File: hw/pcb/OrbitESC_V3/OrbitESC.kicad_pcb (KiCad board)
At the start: 8 copper layers, 39.9 x 25.1 mm, 159 parts, among them J1 USB_C_Receptacle_USB2.0, J11 VDC, J12 GND, J3 TermA, J4 TermB, J5 TermC, J6 CAN1, Q1 MCAC100N08YA-TP, Q2 MCAC100N08YA-TP, Q3 MCAC100N08YA-TP, Q4 MCAC100N08YA-TP, Q5 MCAC100N08YA-TP, Q6 MCAC100N08YA-TP, Q7 2N7002, SW1 Reset, U1 TLE9250X, U10 CP2104, U11 STM32L432KCU6, U12 74HC595BQ, U13 TLV9051IDBVR, U14 TLV9051IDBVR, U2 AT25SF128A-SHB-T, U4 TLV9051IDBVR, U5 DRV8300DRGER, U7 AP62200Z6-7, U8 AP2171W, U9 AP2120

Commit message: save pcb work
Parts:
- added J2: CANH, TestPoint:TestPoint_Pad_1.5x1.5mm, B.Cu at (161.3, 65.5)
- added J7: CANL, TestPoint:TestPoint_Pad_1.5x1.5mm, B.Cu at (161.3, 67.4)
- added J8: RX, TestPoint:TestPoint_Pad_1.5x1.5mm, B.Cu at (166.4, 69.3)
- added J9: TX, TestPoint:TestPoint_Pad_1.5x1.5mm, B.Cu at (164.5, 69.3)
- J6: value CAN1 -> GND; footprint Connector_JST:JST_PH_B3B-PH-K_1x03_P2.00mm_Vertical -> TestPoint:TestPoint_Pad_1.5x1.5mm; moved to B.Cu
- U1, U9: moved to B.Cu
- moved C28 66.9 mm to (172.8, 66.9), turned to -90 degrees
- moved R17 65.8 mm to (169.4, 65.5), turned to 90 degrees
- moved C27 65.6 mm to (171.8, 66.9), turned to 90 degrees
- moved C29 62.3 mm to (168.1, 68.6), turned to -90 degrees
- moved C36 62.0 mm to (167.1, 68.6), turned to 90 degrees
- moved U1 61.9 mm to (165.5, 66.2), turned to 180 degrees
- moved U9 60.2 mm to (169.6, 66.5), turned to 180 degrees
- moved R62 58.2 mm to (162.8, 69.1)
- moved FB1 54.4 mm to (169.4, 68.1), turned to 90 degrees
- moved C10 52.9 mm to (167.6, 66.0), turned to -90 degrees
- moved C26 49.9 mm to (164.3, 70.6)
- moved L3 49.3 mm to (171.7, 65.2)
- moved L2 46.7 mm to (163.3, 66.5)
- moved R37 9.66 mm to (172.7, 88.4), turned to 90 degrees
- moved J6 9.49 mm to (161.3, 69.3), turned to 180 degrees
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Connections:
- J6 pad 1: Net-(J6-Pin_1) -> GND
- R62 pad 1: Net-(J6-Pin_3) -> Net-(J7-Pin_1)
- R62 pad 2: Net-(J6-Pin_1) -> Net-(J2-Pin_1)
- U1 pad 6: Net-(J6-Pin_3) -> Net-(J7-Pin_1)
- U1 pad 7: Net-(J6-Pin_1) -> Net-(J2-Pin_1)
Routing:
- net GND: track 0.00 -> 18.7 mm, vias 12 -> 23
- net CAN1_TXD: track 0.00 -> 11.9 mm
- net VDC: track 0.00 -> 11.6 mm, vias 0 -> 4
- net VBUS: track 0.00 -> 11.4 mm
- net Net-(J1-CC1): track 0.00 -> 8.33 mm, vias 0 -> 1
- net Net-(Q7-D): track 0.00 -> 8.18 mm, vias 0 -> 2
- net Net-(J1-CC2): track 0.00 -> 8.13 mm, vias 0 -> 1
- net +3.3V: track 0.00 -> 6.95 mm, vias 0 -> 2
- net Net-(J2-Pin_1): track 0.00 -> 6.88 mm, vias 0 -> 1
- net SERIAL1_OUT: track 0.00 -> 6.54 mm, vias 0 -> 1
- net Net-(Q7-G): track 0.00 -> 5.90 mm
- net Net-(J7-Pin_1): track 0.00 -> 5.68 mm, vias 0 -> 1
- net CAN1_RXD: track 0.00 -> 5.44 mm
- net Net-(U7-SW): track 0.00 -> 5.06 mm
- net SERIAL1_IN: track 0.00 -> 4.73 mm, vias 0 -> 1
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- added copper zone on F.Cu, net +5V
- added copper zone on F.Cu, net GND
- added copper zone on F.Cu, net Net-(D8-A)
- added copper zone on F.Cu, net VDC
- added copper zone on F.Cu, net VDD
- added copper zone on In3.Cu, net VDD
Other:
- board text added: "CAN"
- board text added: "GND"
- board text added: "H"
- board text added: "L"
- board text added: "RX"
- board text added: "TX"

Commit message: Sync board design
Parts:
- removed D16, D17, D19: Blue LED, Diode_SMD:D_0603_1608Metric
- removed R87, R88, R90: 470, Resistor_SMD:R_0402_1005Metric
- U10, U12: moved to B.Cu
- moved R18 75.4 mm to (209.2, 74.7)
- moved U14 75.4 mm to (205.4, 75.8)
- moved C8 75.1 mm to (209.2, 76.6)
- moved R28 75.0 mm to (211.8, 64.4)
- moved R30 75.0 mm to (211.8, 66.4)
- moved R31 75.0 mm to (211.8, 68.4)
- moved U13 75.0 mm to (204.9, 66.1)
- moved C23 74.1 mm to (209.2, 65.7)
- moved R25 73.5 mm to (206.8, 85.0)
- moved C9 73.3 mm to (206.9, 86.5)
- moved R32 72.3 mm to (209.0, 68.1)
- moved R34 72.2 mm to (211.6, 74.3)
- moved R36 71.8 mm to (211.6, 73.2)
- moved C13 71.5 mm to (205.4, 87.9)
- moved R26 70.6 mm to (204.7, 84.2)
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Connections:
- U12 pad 1: /MCU/Status LEDs/ARMED -> unconnected-(U12-QB-Pad1)
- U12 pad 15: /MCU/Status LEDs/FAULT -> unconnected-(U12-QA-Pad15)
- U12 pad 2: /MCU/Status LEDs/HEARTBEAT -> /MCU/Status LEDs/FAULT
- U12 pad 3: /MCU/Status LEDs/CAN1_ACTV -> /MCU/Status LEDs/ARMED
- U12 pad 4: /MCU/Status LEDs/STATUS_0 -> /MCU/Status LEDs/HEARTBEAT
- U12 pad 5: /MCU/Status LEDs/STATUS_1 -> /MCU/Status LEDs/CAN1_ACTV
- U12 pad 6: /MCU/Status LEDs/STATUS_2 -> unconnected-(U12-QG-Pad6)
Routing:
- net GND: track 18.7 -> 38.3 mm, vias 23 -> 22
- net USB_D+: track 0.00 -> 9.54 mm, vias 0 -> 1
- net USB_D-: track 0.00 -> 9.45 mm, vias 0 -> 1
- net VBUS: track 11.4 -> 19.7 mm, vias 0 -> 1
- net CAN1_TXD: track 11.9 -> 8.32 mm, vias 0 -> 1
- net /MCU/Status LEDs/FAULT: track 0.00 -> 3.24 mm, vias 0 -> 1
- net /MCU/Status LEDs/CAN1_ACTV: track 0.00 -> 3.09 mm, vias 0 -> 1
- net /MCU/Status LEDs/ARMED: track 0.00 -> 2.06 mm, vias 0 -> 1
- net /MCU/Status LEDs/HEARTBEAT: track 0.00 -> 1.91 mm, vias 0 -> 1
- net +3.3V: track 6.95 -> 5.14 mm, vias 2 -> 4
- net SERIAL1_RESET: track 0.00 -> 1.64 mm, vias 0 -> 1
- net Net-(D5-A): track 0.00 -> 1.46 mm
- net Net-(D20-A): track 0.00 -> 1.46 mm
- net Net-(D18-A): track 0.00 -> 1.46 mm
- net Net-(D15-A): track 0.00 -> 1.46 mm
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- added copper zone on In6.Cu, net +3.3V
- added copper zone on In3.Cu, net +3.3VADC
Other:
- board size 39.9 x 25.1 mm -> 34.9 x 25.1 mm

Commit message: sync lunch work
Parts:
- moved C5 102.5 mm to (193.9, 72.0)
- moved C2 100.8 mm to (193.5, 81.9)
- moved R8 99.8 mm to (196.6, 80.1)
- moved R10 99.6 mm to (196.5, 81.4)
- moved R16 99.5 mm to (197.0, 71.2), turned to 90 degrees
- moved R4 97.1 mm to (191.1, 92.2), turned to -90 degrees
- moved R2 93.2 mm to (186.6, 91.9), turned to -90 degrees
- moved R14 87.8 mm to (185.3, 70.7)
- moved C20 62.0 mm to (190.9, 73.9)
- moved C19 61.1 mm to (190.0, 71.1), turned to -90 degrees
- moved C21 55.0 mm to (184.5, 92.1), turned to 90 degrees
- moved C18 47.8 mm to (177.4, 81.4)
- moved C17 40.6 mm to (177.5, 79.5), turned to 180 degrees
- moved U5 32.2 mm to (182.2, 84.3)
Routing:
- net Net-(Q6-G): track 0.00 -> 18.7 mm, vias 0 -> 1
- net /Outputs and Shunts/SH_C: track 0.00 -> 15.3 mm, vias 0 -> 5
- net Net-(Q5-G): track 0.00 -> 12.6 mm, vias 0 -> 1
- net Net-(Q2-G): track 0.00 -> 11.1 mm, vias 0 -> 1
- net Net-(Q4-G): track 0.00 -> 10.9 mm, vias 0 -> 1
- net /Outputs and Shunts/SH_B: track 0.00 -> 8.50 mm, vias 0 -> 5
- net Net-(Q1-G): track 0.00 -> 3.39 mm, vias 0 -> 1
- net Net-(Q3-G): track 0.00 -> 2.47 mm, vias 0 -> 1
- net /Outputs and Shunts/SH_A: vias 0 -> 5

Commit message: sync lunch work
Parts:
- moved R28 24.6 mm to (188.7, 72.9), turned to 90 degrees
- moved R30 24.5 mm to (187.7, 70.9), turned to 90 degrees
- moved R47 24.2 mm to (187.7, 80.5), turned to 90 degrees
- moved C23 22.7 mm to (187.7, 72.9), turned to -90 degrees
- moved C8 22.3 mm to (187.7, 82.5), turned to -90 degrees
- moved R18 21.9 mm to (188.7, 82.5), turned to 90 degrees
- moved C43 21.1 mm to (188.7, 80.5), turned to -90 degrees
- moved C42 21.0 mm to (188.7, 70.9), turned to -90 degrees
- moved R36 20.7 mm to (193.2, 82.5), turned to -90 degrees
- moved R34 18.5 mm to (194.2, 80.5), turned to -90 degrees
- moved R33 18.1 mm to (193.2, 72.9), turned to -90 degrees
- moved R31 17.8 mm to (194.2, 70.9), turned to -90 degrees
- moved R35 17.8 mm to (193.2, 80.5), turned to 90 degrees
- moved R32 16.1 mm to (193.2, 70.9), turned to 90 degrees
- moved U14 15.6 mm to (190.9, 81.5), turned to 90 degrees
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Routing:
- net GND: track 38.3 -> 56.1 mm, vias 22 -> 24
- net Net-(R28-Pad2): track 0.00 -> 9.13 mm, vias 0 -> 2
- net Net-(R18-Pad2): track 0.00 -> 8.93 mm, vias 0 -> 2
- net Net-(U13-+): track 0.00 -> 7.99 mm
- net Net-(U14-+): track 0.00 -> 7.95 mm
- net Net-(U14--): track 0.00 -> 2.94 mm
- net +3.3VADC: track 2.83 -> 5.60 mm, vias 2 -> 4
- net /Outputs and Shunts/A_ISENSE_P: track 0.00 -> 1.52 mm, vias 0 -> 1
- net Net-(U13--): track 0.00 -> 1.50 mm
- net /Outputs and Shunts/B_ISENSE_P: track 0.00 -> 1.48 mm, vias 0 -> 1
- net /MCU/MOTOR_IA: track 0.00 -> 1.03 mm
- net /MCU/MOTOR_IB: track 0.00 -> 1.03 mm

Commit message: Save tonight's PCB work
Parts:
- removed C23: 4.7nF, Capacitor_SMD:C_0402_1005Metric
- removed C55: 100nF, Capacitor_SMD:C_0402_1005Metric
- removed D15, D18: Green LED, Diode_SMD:D_0603_1608Metric
- removed D20: Red LED, Diode_SMD:D_0603_1608Metric
- removed R18, R25, R26, R27, R28, R3, R70, R86, R89: 10k, Resistor_SMD:R_0402_1005Metric
- removed R91: 1.5k, Resistor_SMD:R_0402_1005Metric
- removed TP10: NOR_SCK, TestPoint:TestPoint_Pad_D1.0mm
- removed TP13: NOR_MISO, TestPoint:TestPoint_Pad_D1.0mm
- removed U10: CP2104, Package_DFN_QFN:QFN-24-1EP_4x4mm_P0.5mm_EP2.6x2.6mm
- removed U11: STM32L432KCU6, Package_DFN_QFN:QFN-32-1EP_5x5mm_P0.5mm_EP3.45x3.45mm
- removed U12: 74HC595BQ, Package_DFN_QFN:DHVQFN-16-1EP_2.5x3.5mm_P0.5mm_EP1x2mm
- added C37: 100nF, Capacitor_SMD:C_0402_1005Metric, F.Cu at (177.1, 96.7)
- added C40: 100nF, Capacitor_SMD:C_0402_1005Metric, F.Cu at (203.6, 61.6)
- added C45: 1nF, Capacitor_SMD:C_0402_1005Metric, F.Cu at (209.2, 63.6)
- added C46: 4.7uF, Capacitor_SMD:C_0402_1005Metric, F.Cu at (177.1, 98.7)
- added C47: 100nF, Capacitor_SMD:C_0402_1005Metric, F.Cu at (177.1, 100.6)
- added C48: 100nF, Capacitor_SMD:C_0402_1005Metric, F.Cu at (177.1, 102.6)
- added C49: 100nF, Capacitor_SMD:C_0402_1005Metric, F.Cu at (177.1, 104.6)
- added D4: Yellow LED, Diode_SMD:D_0603_1608Metric, F.Cu at (170.4, 62.7)
- added D6: Green LED, Diode_SMD:D_0603_1608Metric, F.Cu at (174.5, 62.7)
- added D7: Red LED, Diode_SMD:D_0603_1608Metric, F.Cu at (176.5, 62.7)
- added D9: Yellow LED, Diode_SMD:D_0603_1608Metric, F.Cu at (168.4, 62.7)
- added J13: RX, TestPoint:TestPoint_Pad_1.5x1.5mm, B.Cu at (166.4, 69.3)
- added R52: 1.5k, Resistor_SMD:R_0402_1005Metric, F.Cu at (176.5, 60.7)
- added R53: 10k, Resistor_SMD:R_0402_1005Metric, F.Cu at (155.7, 98.7)
- added R54: 10k, Resistor_SMD:R_0402_1005Metric, F.Cu at (155.7, 100.7)
- added R55: 10k, Resistor_SMD:R_0402_1005Metric, F.Cu at (155.7, 102.7)
- added R58: 470, Resistor_SMD:R_0402_1005Metric, F.Cu at (168.4, 60.7)
- added R59: 10k, Resistor_SMD:R_0402_1005Metric, F.Cu at (209.2, 61.6)
- added R60: 1k, Resistor_SMD:R_0402_1005Metric, F.Cu at (208.2, 61.6)
- added R61: 1k, Resistor_SMD:R_0402_1005Metric, F.Cu at (208.2, 63.6)
- added R63: 0.01, Resistor_SMD:R_2512_6332Metric, B.Cu at (205.7, 62.2)
- added R64: 10k, Resistor_SMD:R_0402_1005Metric, F.Cu at (155.7, 106.7)
- added R65: 1k, Resistor_SMD:R_0402_1005Metric, F.Cu at (155.7, 108.6)
- added R66: 1.5k, Resistor_SMD:R_0402_1005Metric, F.Cu at (155.7, 110.6)
- added SW2: DFU, Button_Switch_SMD:SW_SPST_EVQP2, F.Cu at (181.4, 62.3)
- added TP3: NOR_MOSI, TestPoint:TestPoint_Pad_D1.0mm, F.Cu at (173.1, 107.6)
- added TP4: NOR_SCK, TestPoint:TestPoint_Pad_D1.0mm, F.Cu at (173.1, 110.6)
- added TP6: NOR_MISO, TestPoint:TestPoint_Pad_D1.0mm, F.Cu at (173.1, 113.7)
- added U3: STM32F446RETx, Package_QFP:LQFP-64_10x10mm_P0.5mm, F.Cu at (180.8, 78.4)
- added U6: TLV9051IDBVR, Package_TO_SOT_SMD:SOT-23-5, F.Cu at (205.9, 62.6)
- added X1: ASE-24MHz, Oscillator:Oscillator_SMD_Abracon_ASE-4Pin_3.2x2.5mm, F.Cu at (166.4, 112.4)
- C4, C7: value 47uF -> 100nF; footprint Capacitor_SMD:C_0805_2012Metric -> Capacitor_SMD:C_0402_1005Metric
- C8: value 4.7nF -> 4.7uF
- D5: value Yellow LED -> Green LED
- J8: value RX -> Micro_SD_Card_Det2; footprint TestPoint:TestPoint_Pad_1.5x1.5mm -> Connector_Card:microSD_HC_Hirose_DM3D-SF
- R15: value 100k -> 120
- R42, R62: value 120 -> 10k
- SW1: footprint Button_Switch_SMD:SW_SPST_PTS810 -> Button_Switch_SMD:SW_SPST_EVQP2
- TP2: value NOR_MISO -> NOR_nCS
- TP5: value NOR_nCS -> NOR_MISO
- TP9: value NOR_MOSI -> AH
- moved R29 53.8 mm to (174.5, 60.7), turned to 180 degrees
- moved R19 51.0 mm to (172.5, 60.7), turned to 180 degrees
- moved R62 40.5 mm to (202.6, 61.6), turned to 90 degrees
- moved C18 37.5 mm to (208.7, 102.2)
- moved C17 37.3 mm to (208.4, 100.5)
- moved C20 35.8 mm to (209.6, 98.7)
- moved R10 32.7 mm to (213.9, 109.1)
- moved R8 31.5 mm to (213.4, 106.8)
- moved R14 20.8 mm to (201.4, 57.5)
- moved U5 19.5 mm to (199.3, 93.8)
- moved C19 19.4 mm to (195.2, 93.0)
- moved C9 15.6 mm to (215.6, 99.4)
- moved R46 15.6 mm to (216.3, 102.5)
- moved R49 15.6 mm to (217.9, 99.4)
- moved R51 15.6 mm to (217.8, 96.4)
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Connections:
- net VS renamed VSUPPLY
- C13 pad 2: Net-(C13-Pad2) -> /Outputs and Shunts/SH_B
- C22 pad 2: Net-(C22-Pad2) -> /Outputs and Shunts/SH_C
- C32 pad 2: +3.3V -> nDFU_BOOT
- C4 pad 1: VBUS -> GND
- C4 pad 2: GND -> +3.3V
- C7 pad 1: Net-(U10-VPP) -> GND
- C7 pad 2: GND -> +3.3V
- C8 pad 2: /MCU/MOTOR_IA -> +3.3V
- C9 pad 2: Net-(C9-Pad2) -> /Outputs and Shunts/SH_A
- J10 pad 1: Net-(J10-Pin_1) -> +3.3V
- J8 pad 1: SERIAL1_IN -> SDIO_D2
- Q6 pad 3: GND -> /Outputs and Shunts/C_ISENSE_P
- R15 pad 1: SERIAL1_RESET -> Net-(J7-Pin_1)
- R15 pad 2: +3.3V -> Net-(J2-Pin_1)
- R19 pad 1: GND -> HeartbeatLED
- R19 pad 2: LED_nOE -> Net-(D5-A)
- R29 pad 1: LED_nCS -> ArmedLED
- R29 pad 2: +3.3V -> Net-(D6-A)
- R31 pad 1: Net-(R28-Pad2) -> /MCU/MOTOR_IB
- R34 pad 1: Net-(R18-Pad2) -> /MCU/MOTOR_IA
- R42 pad 1: Net-(J10-Pin_1) -> GND
- R42 pad 2: +3.3V -> nDFU_BOOT
- R45 pad 2: Net-(C9-Pad2) -> /Outputs and Shunts/SH_A
- R49 pad 2: Net-(C13-Pad2) -> /Outputs and Shunts/SH_B
- R51 pad 2: Net-(C22-Pad2) -> /Outputs and Shunts/SH_C
- R62 pad 1: Net-(J7-Pin_1) -> Net-(U6-+)
- R62 pad 2: Net-(J2-Pin_1) -> ISenseVRef
- R7 pad 1: /MCU/Status LEDs/CAN1_ACTV -> CANActiveLED
- R7 pad 2: Net-(D5-A) -> Net-(D4-A)
- TP2 pad 1: GND -> NOR_nCS
- TP5 pad 1: NOR_nCS -> GND
- TP9 pad 1: NOR_MOSI -> /MCU/MOTOR_IC
- U13 pad 1: Net-(R28-Pad2) -> /MCU/MOTOR_IB
- U14 pad 1: Net-(R18-Pad2) -> /MCU/MOTOR_IA
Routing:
- net Net-(Q6-G): track 18.7 -> 0.00 mm
- net /Outputs and Shunts/SH_C: track 15.3 -> 0.00 mm
- net Net-(Q5-G): track 12.6 -> 0.76 mm
- net Net-(Q2-G): track 11.1 -> 0.00 mm
- net Net-(Q4-G): track 10.9 -> 0.00 mm
- net Net-(R28-Pad2): track 9.13 -> 0.00 mm, vias 2 -> 0
- net Net-(R18-Pad2): track 8.93 -> 0.00 mm, vias 2 -> 0
- net /Outputs and Shunts/SH_B: track 8.50 -> 0.00 mm
- net VBUS: track 19.7 -> 11.4 mm, vias 1 -> 0
- net USB_D+: track 9.54 -> 1.70 mm, vias 1 -> 0
- net USB_D-: track 9.45 -> 1.70 mm, vias 1 -> 0
- net /MCU/MOTOR_IB: track 1.03 -> 7.66 mm, vias 0 -> 2
- net /MCU/MOTOR_IA: track 1.03 -> 7.46 mm, vias 0 -> 2
- net GND: track 56.1 -> 52.0 mm, vias 24 -> 20
- net Net-(Q1-G): track 3.39 -> 0.00 mm
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- added copper zone on B.Cu, net /Outputs and Shunts/C_ISENSE_P
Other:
- board size 34.9 x 25.1 mm -> 49.9 x 29.2 mm

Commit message: Possible rough new component placement
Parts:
- U2: moved to B.Cu
- moved C39 73.5 mm to (178.6, 52.5)
- moved C41 73.5 mm to (178.6, 54.5)
- moved R23 73.5 mm to (167.1, 52.5)
- moved R24 73.5 mm to (167.1, 54.5)
- moved R42 73.5 mm to (167.1, 56.5)
- moved TH1 73.5 mm to (170.0, 56.5)
- moved C1 73.5 mm to (172.8, 52.5)
- moved C11 73.5 mm to (175.7, 52.5)
- moved C15 73.5 mm to (175.7, 54.5)
- moved C3 73.5 mm to (172.8, 54.5)
- moved TP5 73.5 mm to (161.2, 49.6)
- moved TP9 73.5 mm to (161.2, 52.6)
- moved C35 73.5 mm to (175.7, 56.5)
- moved C6 73.5 mm to (172.8, 56.5)
- moved R1 73.5 mm to (164.1, 52.5)
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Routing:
- net GND: track 52.0 -> 43.4 mm, vias 20 -> 21
- net /MCU/MOTOR_IC: track 0.00 -> 6.94 mm
- net Net-(U6-+): track 1.50 -> 6.39 mm
- net Net-(U13-+): track 7.99 -> 6.39 mm
- net Net-(U14-+): track 7.95 -> 6.39 mm
- net /Outputs and Shunts/B_ISENSE_P: track 1.48 -> 2.80 mm
- net /Outputs and Shunts/A_ISENSE_P: track 1.52 -> 2.84 mm
- net /Outputs and Shunts/C_ISENSE_P: track 1.48 -> 2.80 mm
- net /MCU/MOTOR_IB: track 7.66 -> 6.94 mm, vias 2 -> 0
- net /MCU/MOTOR_IA: track 7.46 -> 6.87 mm, vias 2 -> 0

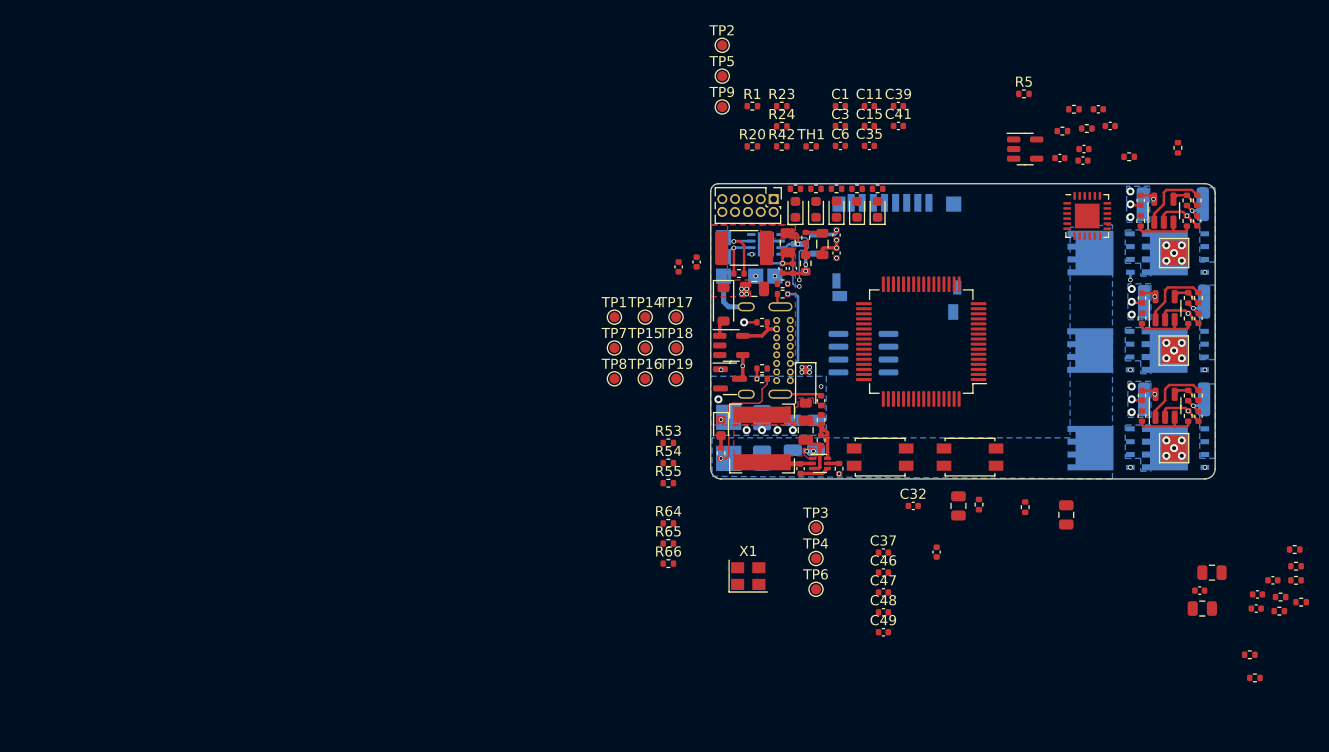
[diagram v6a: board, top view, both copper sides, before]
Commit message: Finish initial draft of V3 pcb
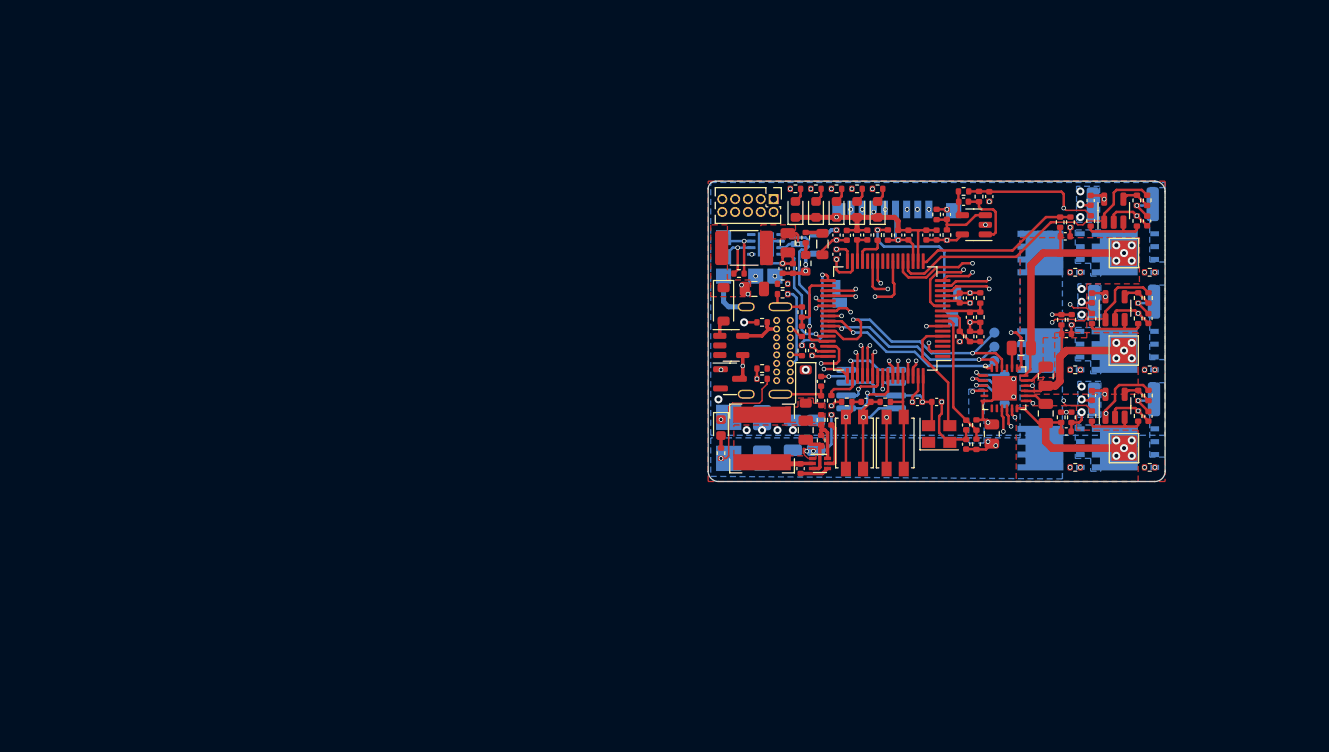
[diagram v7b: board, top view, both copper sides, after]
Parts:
- removed C32, C4: 100nF, Capacitor_SMD:C_0402_1005Metric
- removed TP1: BL, TestPoint:TestPoint_Pad_D1.0mm
- removed TP2: NOR_nCS, TestPoint:TestPoint_Pad_D1.0mm
- removed TP3: NOR_MOSI, TestPoint:TestPoint_Pad_D1.0mm
- removed TP4: NOR_SCK, TestPoint:TestPoint_Pad_D1.0mm
- removed TP5, TP6: NOR_MISO, TestPoint:TestPoint_Pad_D1.0mm
- removed TP7, TP8, TP9: AH, TestPoint:TestPoint_Pad_D1.0mm
- added R56: 56k, Resistor_SMD:R_0402_1005Metric, F.Cu at (169.0, 74.8)
- added R57: 100k, Resistor_SMD:R_0402_1005Metric, F.Cu at (169.0, 72.9)
- TP14, TP15, TP16, TP17, TP18, TP19: moved to B.Cu
- moved R50 44.0 mm to (195.6, 64.0), turned to -90 degrees
- moved C22 41.4 mm to (195.1, 65.4), turned to 180 degrees
- moved R51 39.8 mm to (194.6, 64.0), turned to -90 degrees
- moved C49 39.4 mm to (179.6, 65.3), turned to -90 degrees
- moved R23 38.6 mm to (186.3, 86.0), turned to -90 degrees
- moved R65 36.9 mm to (176.5, 65.3), turned to 90 degrees
- moved R64 35.9 mm to (177.5, 65.3), turned to -90 degrees
- moved C48 35.7 mm to (172.5, 67.2), turned to 90 degrees
- moved TP15 35.7 mm to (189.1, 79.1), turned to 180 degrees
- moved C47 35.4 mm to (175.5, 65.3), turned to 90 degrees
- moved R24 35.3 mm to (186.3, 84.1), turned to 90 degrees
- moved TP16 34.7 mm to (188.1, 76.3), turned to 180 degrees
- moved R49 34.7 mm to (194.7, 73.7), turned to -90 degrees
- moved TP14 34.6 mm to (188.1, 74.9), turned to 180 degrees
- moved C46 33.5 mm to (174.5, 65.3), turned to -90 degrees
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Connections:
- U3 pad 10: VMCU -> VTEMP
- U3 pad 15: /MCU/MOTOR_IB -> /MCU/MOTOR_VA
- U3 pad 16: /MCU/MOTOR_IC -> /MCU/MOTOR_IB
- U3 pad 17: /MCU/MOTOR_VA -> /MCU/MOTOR_VC
- U3 pad 2: USBActiveLED -> FaultLED
- U3 pad 20: /MCU/MOTOR_VB -> /MCU/MOTOR_IC
- U3 pad 21: /MCU/MOTOR_VC -> /MCU/MOTOR_VB
- U3 pad 58: FaultLED -> ArmedLED
- U3 pad 59: ArmedLED -> HeartbeatLED
- U3 pad 61: HeartbeatLED -> CANActiveLED
- U3 pad 62: CANActiveLED -> USBActiveLED
- U3 pad 9: VTEMP -> VMCU
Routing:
- net GND: track 43.4 -> 114.5 mm, vias 21 -> 37
- net ISenseVRef: track 0.00 -> 57.8 mm, vias 0 -> 4
- net nRESET: track 0.00 -> 56.7 mm, vias 0 -> 2
- net SWDIO: track 0.00 -> 38.7 mm, vias 0 -> 1
- net USBActiveLED: track 0.00 -> 37.2 mm, vias 0 -> 2
- net +3.3V: track 5.13 -> 41.4 mm, vias 3 -> 11
- net SWCLK: track 0.00 -> 35.6 mm, vias 0 -> 1
- net CANActiveLED: track 0.00 -> 30.2 mm, vias 0 -> 2
- net /MCU/MOTOR_IA: track 6.87 -> 35.0 mm, vias 0 -> 2
- net HeartbeatLED: track 0.00 -> 28.1 mm, vias 0 -> 2
- net /Outputs and Shunts/GDL_B: track 0.00 -> 27.8 mm, vias 0 -> 2
- net /Outputs and Shunts/GDL_C: track 0.00 -> 27.7 mm, vias 0 -> 2
- net ArmedLED: track 0.00 -> 26.8 mm, vias 0 -> 2
- net /MCU/GATE_DRIVE_CH: track 0.00 -> 26.1 mm, vias 0 -> 2
- net /MCU/MOTOR_VA: track 0.00 -> 25.2 mm, vias 0 -> 2
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- added copper zone on F.Cu, net /Outputs and Shunts/SH_A
- added copper zone on F.Cu, net /Outputs and Shunts/SH_B
- added copper zone on F.Cu, net /Outputs and Shunts/SH_C
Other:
- board size 49.9 x 29.2 mm -> 45.2 x 29.7 mm
- board text added: "AH"
- board text added: "AL"
- board text added: "BH"
- board text added: "BL"
- board text added: "CH"
- board text added: "CL"
